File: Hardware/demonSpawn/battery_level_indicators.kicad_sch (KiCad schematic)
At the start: 16 parts

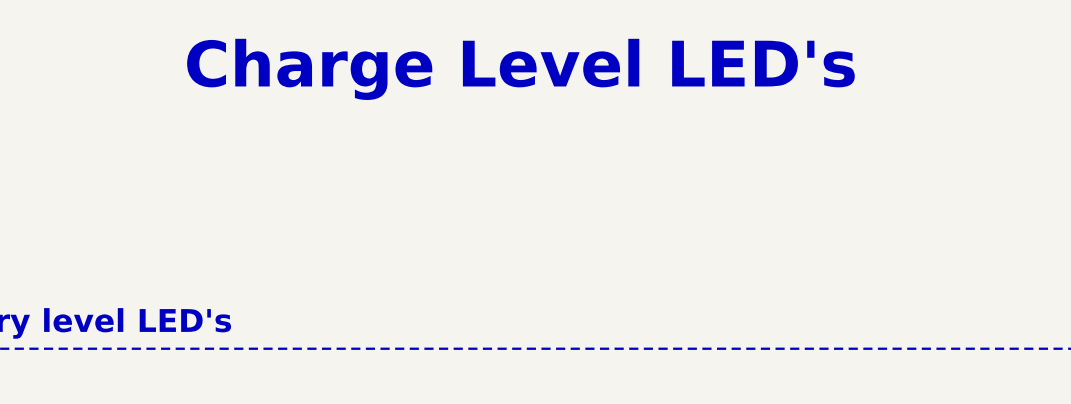
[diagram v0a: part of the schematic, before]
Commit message: doc: Add schematic pdf
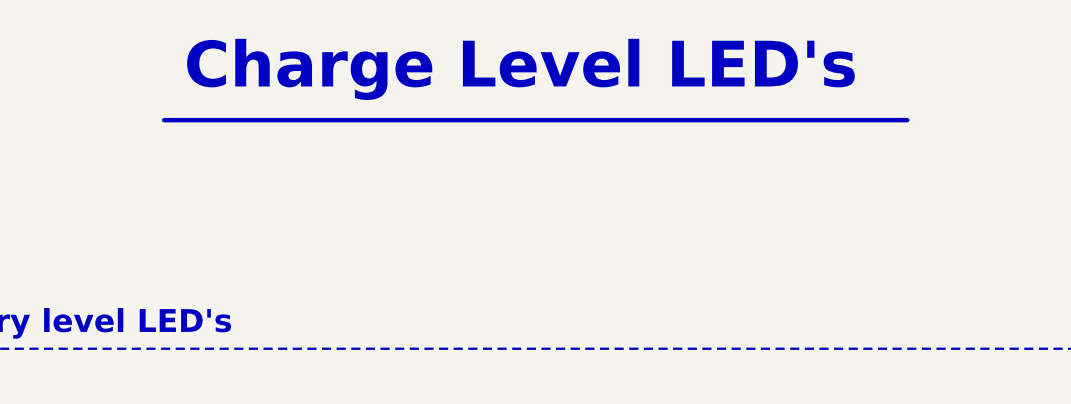
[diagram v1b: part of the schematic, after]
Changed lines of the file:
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@@
+		)
+	)
+	(polyline
+		(pts
+			(xy 115.57 25.4) (xy 198.12 25.4)
+		)
+		(stroke
+			(width 0.5)
+			(type solid)
 		)
 	)
